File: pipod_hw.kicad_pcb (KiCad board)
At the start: 4 copper layers, 55.5 x 96.8 mm, 177 parts, among them J1 Conn_01x03_Male, J2 USB_C_Receptacle_USB2.0, J3 SFV8R-2STE1HLF, J4 SFV14R-2STE1HLF, J5 2-1734839-5, J6 S7051-42R, J7 S7051-42R, Q1 DMG9926UDM, Q2 NTK3139PT1G, Q3 BSS138, SW1 SW_Push, SW2 SW_Push, U1 MAX17048G+T10, U10 TPS22965TDSGRQ1, U11 TPS22965TDSGRQ1, U12 TPS22965TDSGRQ1, U13 PCM5102APWR, U14 PAM8908JER, U15 MCP23008-E/ML, U2 MAX8903AETI+T, U3 BQ29728DSER, U4 XC6210B332MR, U5 W25Q128JVS, U6 RP2040, U7 NLAS7242MUTBG, U8 RS2299XTQC16, U9 TPS22965TDSGRQ1, Y1 12MHz 20pF

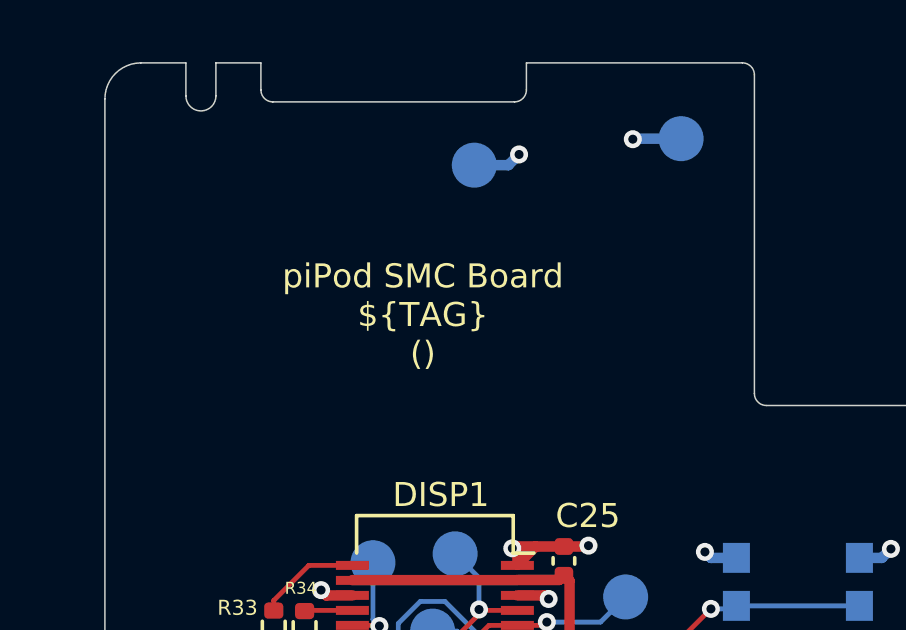
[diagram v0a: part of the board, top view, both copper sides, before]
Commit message: layout: add OSHW logo, change version text to masked copper
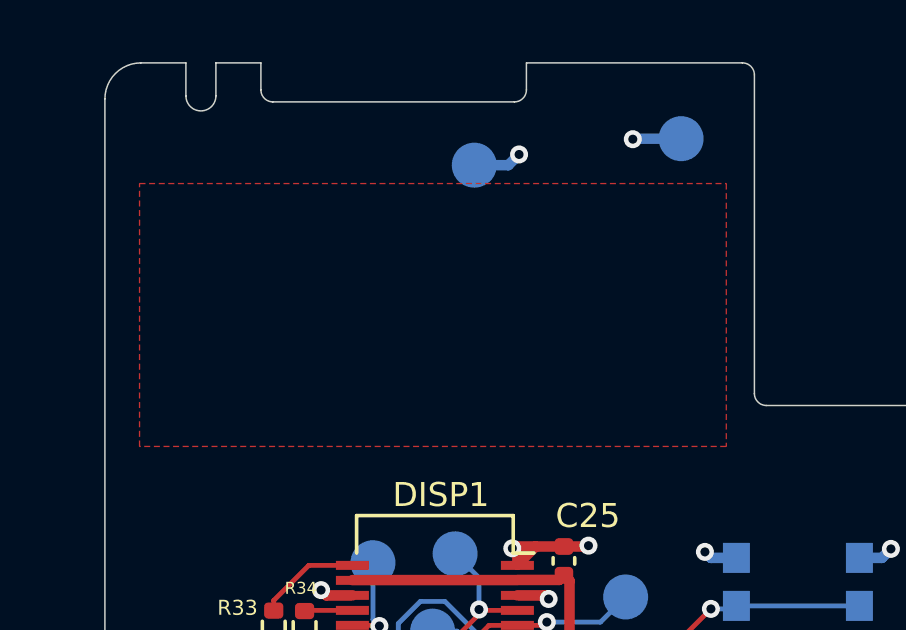
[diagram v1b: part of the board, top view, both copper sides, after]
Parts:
- added LOGO1: Logo_Open_Hardware_Large, Gigahawk:OSHW-Logo2_9.8x8mm_Mask, F.Cu at (6.23, 8.47)
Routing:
- added copper zone on F.Cu, net (none)

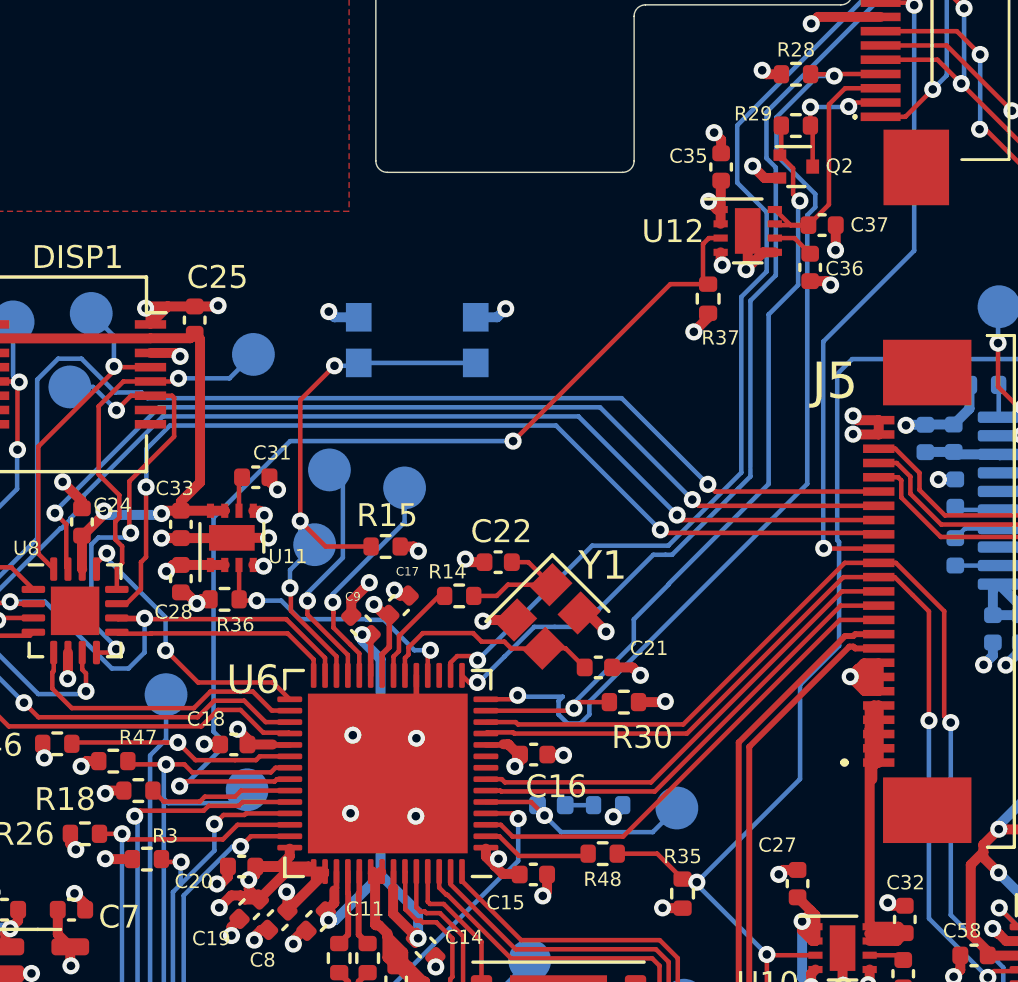
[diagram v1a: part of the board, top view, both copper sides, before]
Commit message: feature: add hardware ID resistors
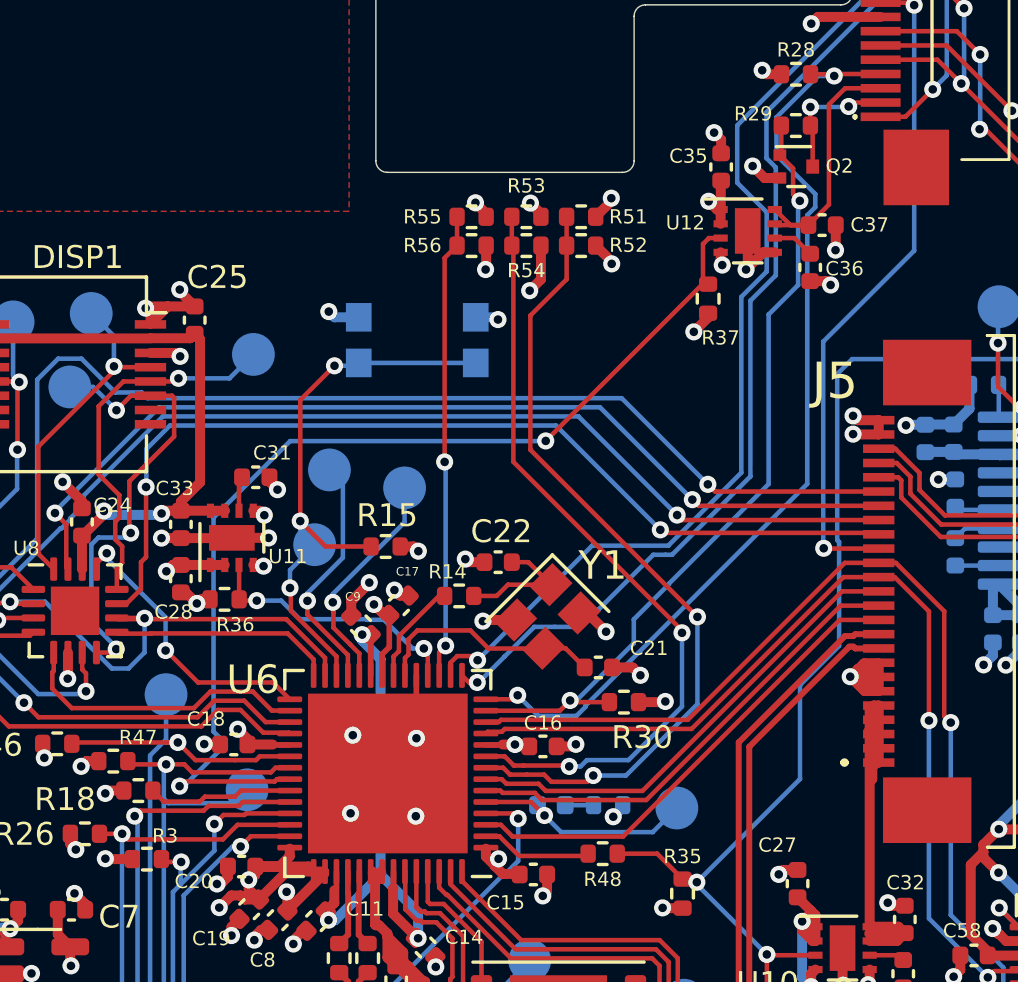
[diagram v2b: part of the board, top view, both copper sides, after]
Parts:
- added R51: DNI, Resistor_SMD:R_0402_1005Metric, F.Cu at (28.8, 13.0)
- added R52: 10k, Resistor_SMD:R_0402_1005Metric, F.Cu at (28.8, 14.0)
- added R53: DNI, Resistor_SMD:R_0402_1005Metric, F.Cu at (26.9, 13.0)
- added R54: 10k, Resistor_SMD:R_0402_1005Metric, F.Cu at (26.9, 14.0)
- added R55: DNI, Resistor_SMD:R_0402_1005Metric, F.Cu at (25.0, 13.0)
- added R56: 10k, Resistor_SMD:R_0402_1005Metric, F.Cu at (25.0, 14.0)
- moved C16 0.43 mm to (27.5, 31.5)
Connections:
- U6 pad 17: unconnected-(U6-Pad17) -> HWID2
- U6 pad 8: unconnected-(U6-Pad8) -> HWID0
- U6 pad 9: unconnected-(U6-Pad9) -> HWID1
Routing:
- net HWID0: track 0.00 -> 28.8 mm, vias 0 -> 2
- net HWID1: track 0.00 -> 27.5 mm, vias 0 -> 2
- net HWID2: track 0.00 -> 16.4 mm, vias 0 -> 2
- net GND: track 148.0 -> 151.2 mm, vias 112 -> 115
- net +3V3: track 60.2 -> 62.1 mm, vias 30 -> 33
- net HP_LCK: track 34.7 -> 33.7 mm
